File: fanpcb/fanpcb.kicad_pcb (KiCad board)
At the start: 2 copper layers, 30 x 50 mm, 18 parts, among them M1 Fan_4pin, M2 Fan_4pin, M3 Fan_4pin, T1 TACHO, T12V1 TestPoint, T2 TACHO, T3 TACHO

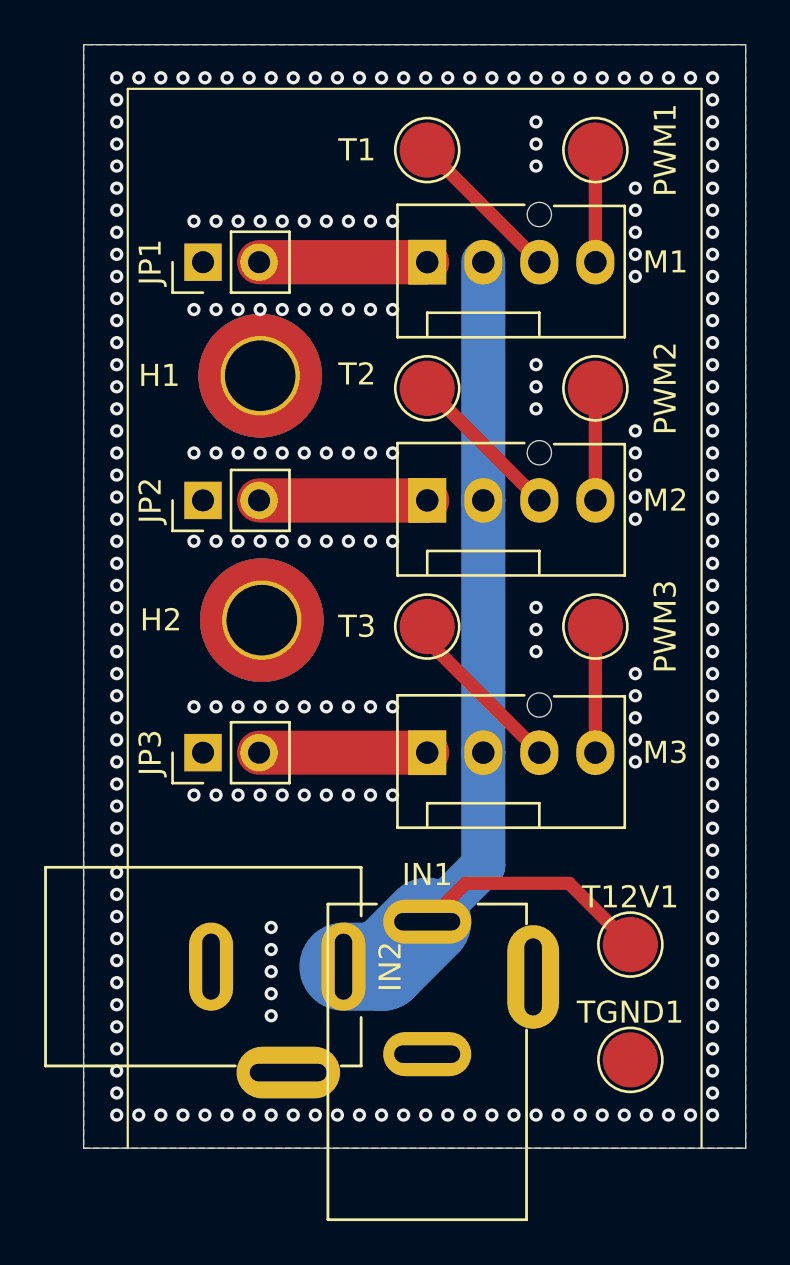
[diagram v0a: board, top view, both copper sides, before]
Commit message: fanpcb freewheelingdiods and smoothingcapacitors
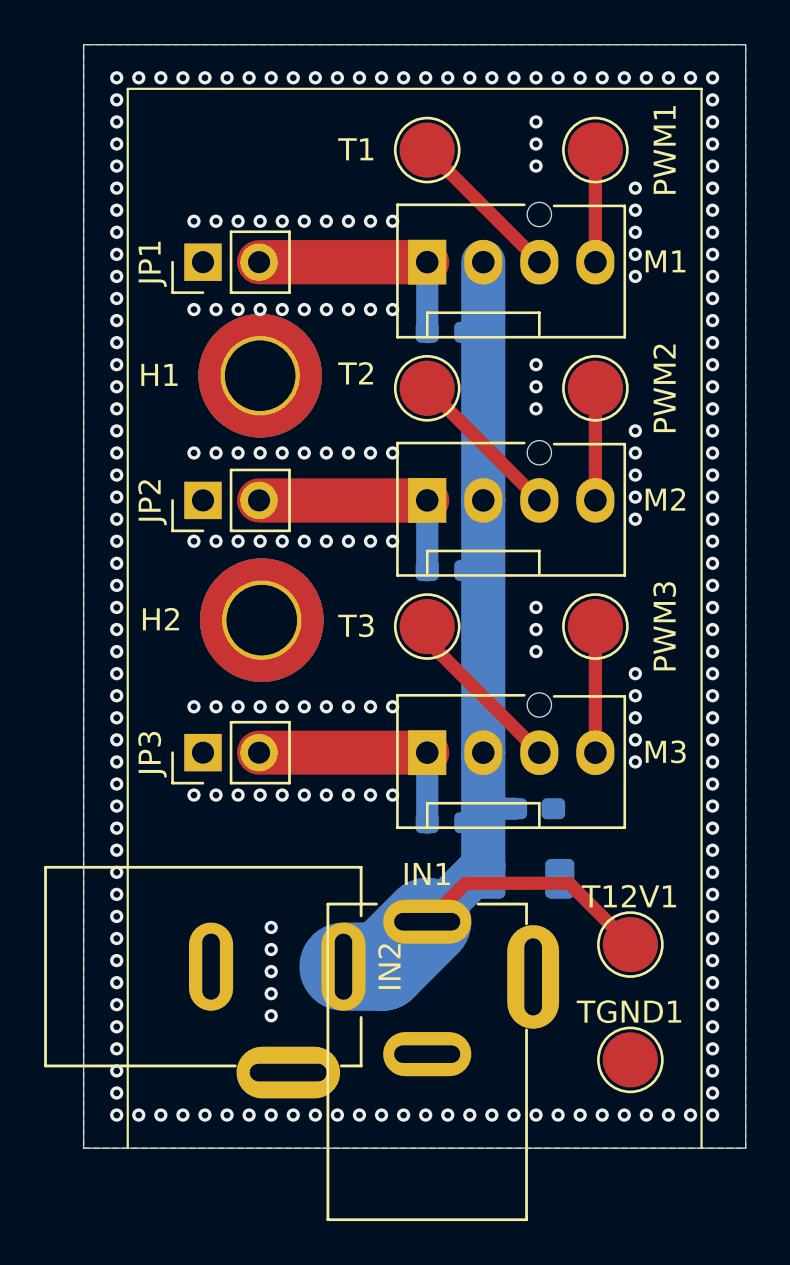
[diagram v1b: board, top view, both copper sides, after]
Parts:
- added C1: C, Capacitor_SMD:C_1206_3216Metric_Pad1.33x1.80mm_HandSolder, B.Cu at (120.0, 137.8)
- added C2: C, Capacitor_SMD:C_0603_1608Metric_Pad1.08x0.95mm_HandSolder, B.Cu at (120.4, 134.6)
- added D1: D, Diode_SMD:D_0603_1608Metric_Pad1.05x0.95mm_HandSolder, B.Cu at (116.4, 113.0)
- added D2: D, Diode_SMD:D_0603_1608Metric_Pad1.05x0.95mm_HandSolder, B.Cu at (116.4, 123.8)
- added D3: D, Diode_SMD:D_0603_1608Metric_Pad1.05x0.95mm_HandSolder, B.Cu at (116.4, 135.3)
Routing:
- net Net-(D2-A): track 7.62 -> 10.8 mm
- net Net-(D1-A): track 7.62 -> 10.8 mm
- net Net-(D3-A): track 7.62 -> 10.8 mm
- net +12V: track 46.7 -> 48.1 mm
